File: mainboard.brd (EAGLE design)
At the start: 90.2 x 95.9 mm, 6 parts, among them U1 ATMEGA2560AU, U2 ITG-3200

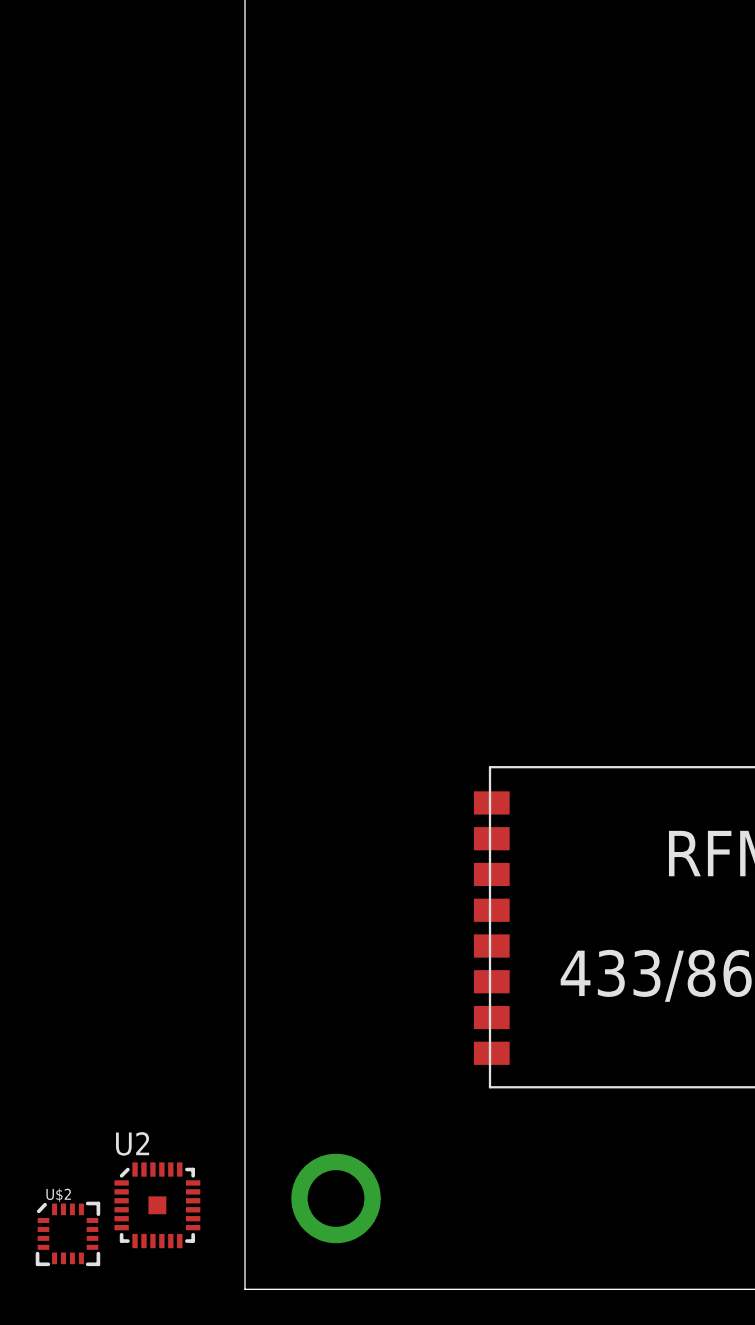
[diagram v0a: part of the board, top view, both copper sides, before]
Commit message: rename main board
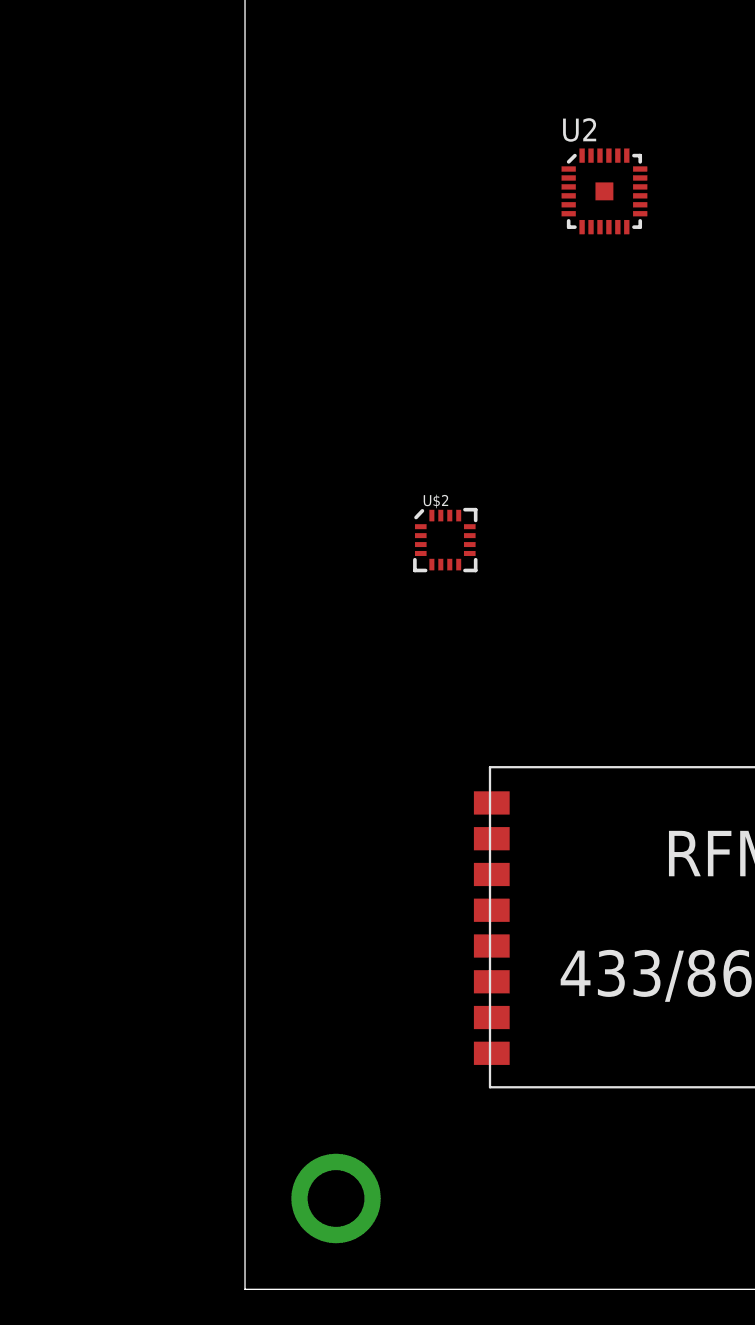
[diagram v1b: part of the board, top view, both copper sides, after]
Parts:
- moved U2 62.0 mm to (20.1, 61.4)
- moved U$2 44.2 mm to (11.2, 41.9)
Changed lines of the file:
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@@
 <element name="U1" library="SparkFun-DigitalIC" package="TQFP100" value="ATMEGA2560AU" x="45.7" y="44.1"/>
 <element name="U$1" library="RFM23BP" package="RFM23BP" value="RFM23BP" x="29.7" y="20.7"/>
-<element name="U2" library="SparkFun-Sensors" package="QFN-24" value="ITG-3200" x="-4.9" y="4.7"/>
-<element name="U$2" library="SparkFun-Sensors" package="16LPCC" value="HMC5883LSMD" x="-9.9" y="3.1"/>
+<element name="U2" library="SparkFun-Sensors" package="QFN-24" value="ITG-3200" x="20.1" y="61.4"/>
+<element name="U$2" library="SparkFun-Sensors" package="16LPCC" value="HMC5883LSMD" x="11.2" y="41.9"/>
 </elements>
 <signals>

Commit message: Added documentation
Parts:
- added IC1: FT232RLSSOP, SparkFun:SSOP28DB
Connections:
- new net GND18: IC1.18
- new net GND21: IC1.21
- new net GND7: IC1.7
- new net VCCIO: IC1.4
- net AGND: now also IC1.25
- net VCC: now also IC1.20
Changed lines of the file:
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@@
 <element name="U2" library="SparkFun-Sensors" package="QFN-24" value="ITG-3200" x="20.1" y="61.4"/>
 <element name="U$2" library="SparkFun-Sensors" package="16LPCC" value="HMC5883LSMD" x="11.2" y="41.9"/>
+<element name="IC1" library="SparkFun" package="SSOP28DB" value="FT232RLSSOP" x="66.2" y="61.6"/>
 </elements>
 <signals>
@@
 <signal name="AGND">
 <contactref element="U1" pad="99"/>
+<contactref element="IC1" pad="25"/>
+<wire x1="63.925" y1="65.256" x2="40.2" y2="52.1" width="0" layer="19" extent="1-1"/>
 </signal>
 <signal name="AVCC">
@@
 <contactref element="U1" pad="10"/>
 <contactref element="U$1" pad="VCC"/>
+<contactref element="IC1" pad="20"/>
 <wire x1="46.6" y1="21.2" x2="37.7" y2="45.6" width="0" layer="19" extent="1-1"/>
+<wire x1="67.175" y1="65.256" x2="46.6" y2="21.2" width="0" layer="19" extent="1-1"/>
 </signal>
 <signal name="VCC1">
@@
 <contactref element="U1" pad="80"/>
 </signal>
+<signal name="GND7">
+<contactref element="IC1" pad="7"/>
+</signal>
+<signal name="GND18">
+<contactref element="IC1" pad="18"/>
+</signal>
+<signal name="GND21">
+<contactref element="IC1" pad="21"/>
+</signal>
+<signal name="VCCIO">
+<contactref element="IC1" pad="4"/>
+</signal>
 </signals>

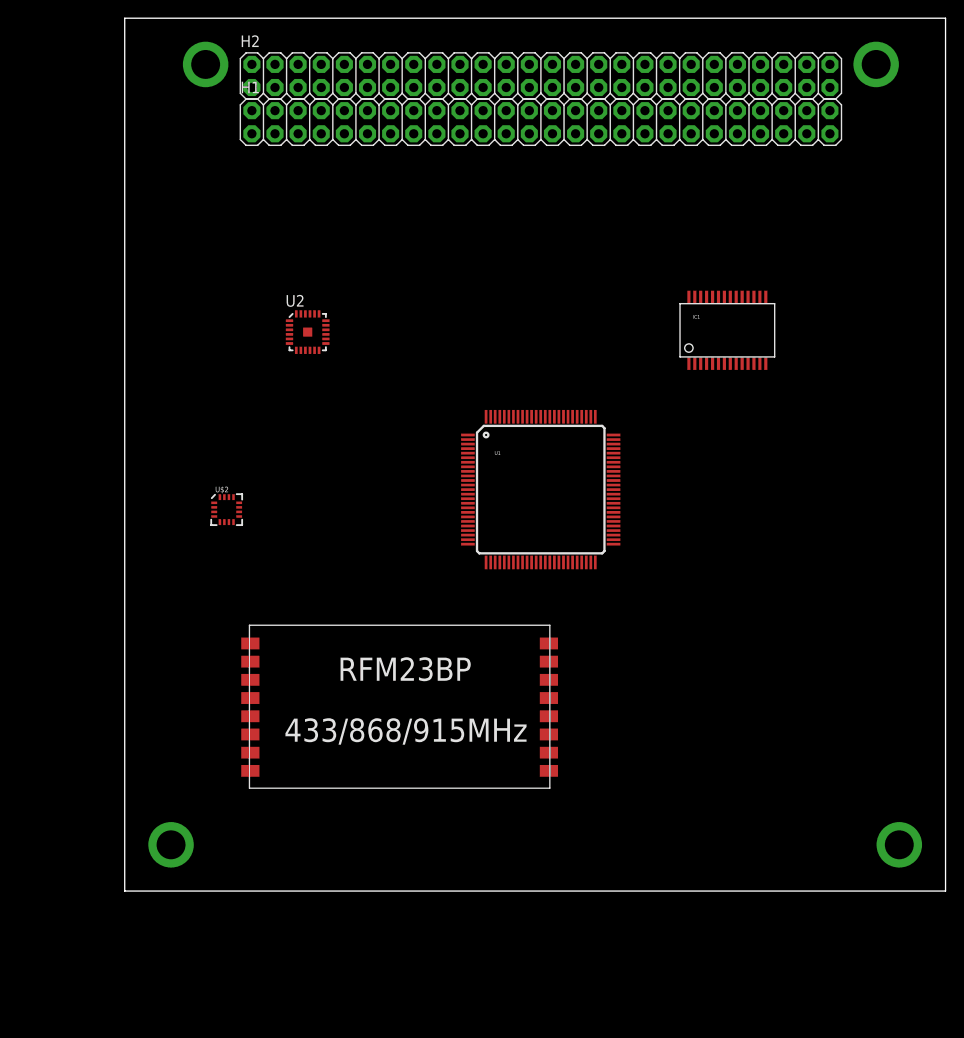
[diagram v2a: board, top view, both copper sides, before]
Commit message: Mitered corners of mainboard
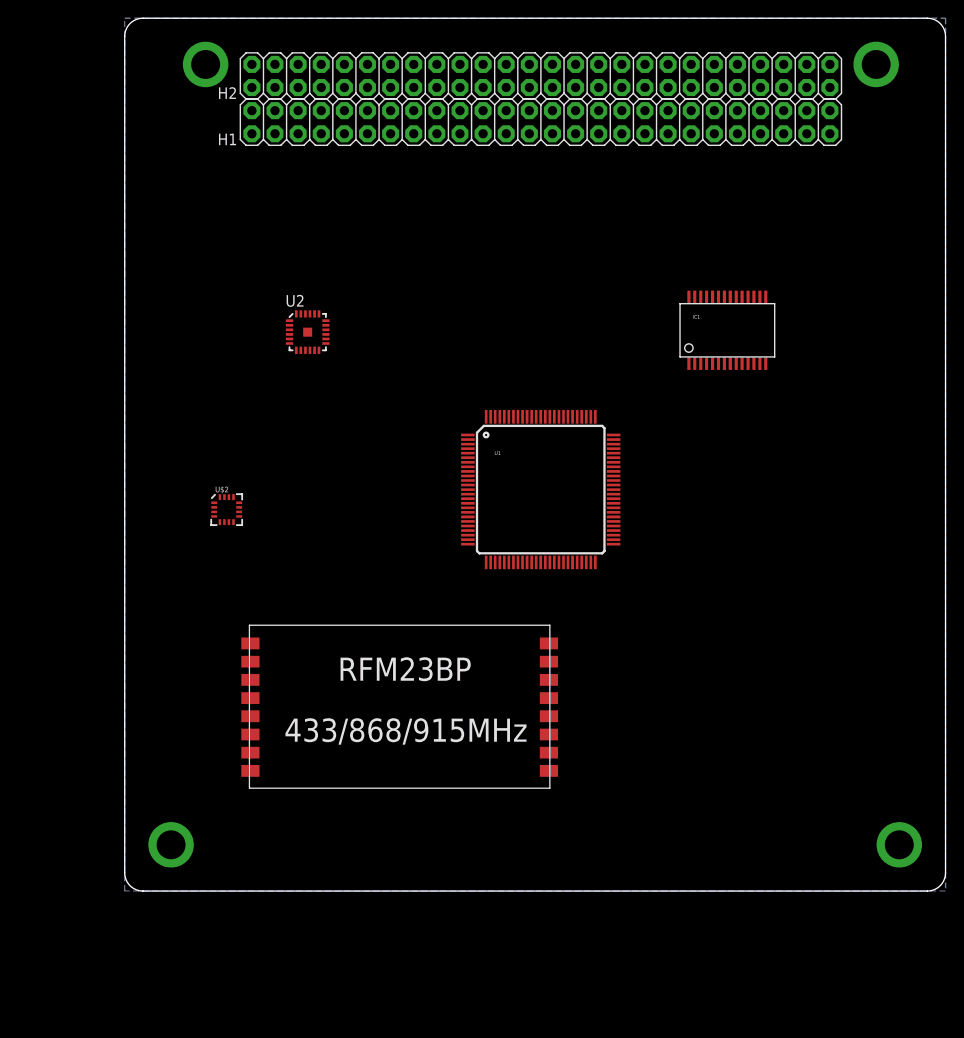
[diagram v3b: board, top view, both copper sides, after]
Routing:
- added copper zone on layer 16, net GND
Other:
- outline, holes or cut-outs redrawn
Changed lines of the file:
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@@
 <board>
 <plain>
-<wire x1="0" y1="0" x2="90.17" y2="0" width="0" layer="20"/>
-<wire x1="90.17" y1="0" x2="90.17" y2="95.885" width="0" layer="20"/>
-<wire x1="90.17" y1="95.885" x2="0" y2="95.885" width="0" layer="20"/>
-<wire x1="0" y1="95.885" x2="0" y2="0" width="0" layer="20"/>
+<wire x1="0" y1="93.885" x2="0" y2="2" width="0" layer="20"/>
+<wire x1="0" y1="2" x2="2" y2="0" width="0" layer="20" curve="90"/>
+<wire x1="2" y1="0" x2="88.17" y2="0" width="0" layer="20"/>
+<wire x1="88.17" y1="0" x2="90.17" y2="2" width="0" layer="20" curve="90"/>
+<wire x1="90.17" y1="2" x2="90.17" y2="93.885" width="0" layer="20"/>
+<wire x1="90.17" y1="93.885" x2="88.17" y2="95.885" width="0" layer="20" curve="90"/>
+<wire x1="88.17" y1="95.885" x2="2" y2="95.885" width="0" layer="20"/>
+<wire x1="2" y1="95.885" x2="0" y2="93.885" width="0" layer="20" curve="90"/>
 </plain>
 <attributes>
@@
 </class>
 </classes>
-<designrules name="default">
-<description language="de">&lt;b&gt;EAGLE Design Rules&lt;/b&gt;
+<designrules name="SSC-EAGLE-2Lyr_v1.0.0.3">
+<description language="en">&lt;b&gt;EAGLE Design Rules for *2* Layer Designs (DS)&lt;/b&gt;
 &lt;p&gt;
-Die Standard-Design-Rules sind so gewählt, dass sie für
-die meisten Anwendungen passen. Sollte ihre Platine
-besondere Anforderungen haben, treffen Sie die erforderlichen
-Einstellungen hier und speichern die Design Rules unter
-einem neuen Namen ab.</description>
-<description language="en">&lt;b&gt;EAGLE Design Rules&lt;/b&gt;
+This Sunstone Circuits 2 Layer .DRU has been set to cover our minimum requirements for our double sided products. For questions, comments, suggestions, please contact Sunstone Customer Support: &lt;p&gt;&lt;b&gt;Email:&lt;/b&gt;  mailto:support@sunstone.com&lt;br&gt;&lt;b&gt;Phone:&lt;/b&gt; 800-228-8198.&lt;p&gt; v1.1Mod10/16/07~Layers-core reversal.Distance C/D.Restring%.Supply G%.&lt;p&gt; v1.2 Mod12/06/07~Distance C/D to 20mils.&lt;p&gt;v1.3Mod12/12/07~Supply/Annulus Value to 12.5mils&lt;p&gt;1/15/08 SSC-EAGLE-2Lyr_v1.0.0.3~For Release&lt;p&gt;10/3/08 Description Edit.&lt;p&gt;
 &lt;p&gt;
-The default Design Rules have been set to cover
-a wide range of applications. Your particular design
-may have different requirements, so please make the
-necessary adjustments and save your customized
-design rules under a new name.</description>
+&lt;i&gt;Attention: Upon running the design check and making modifications, please remember to save any changes before closing the application and sending in your board file to Sunstone Circuits for conversion.&lt;i&gt;</description>
 <param name="layerSetup" value="(1*16)"/>
-<param name="mtCopper" value="0.035mm 0.035mm 0.035mm 0.035mm 0.035mm 0.035mm 0.035mm 0.035mm 0.035mm 0.035mm 0.035mm 0.035mm 0.035mm 0.035mm 0.035mm 0.035mm"/>
-<param name="mtIsolate" value="1.5mm 0.15mm 0.2mm 0.15mm 0.2mm 0.15mm 0.2mm 0.15mm 0.2mm 0.15mm 0.2mm 0.15mm 0.2mm 0.15mm 0.2mm"/>
-<param name="mdWireWire" value="8mil"/>
-<param name="mdWirePad" value="8mil"/>
-<param name="mdWireVia" value="8mil"/>
-<param name="mdPadPad" value="8mil"/>
-<param name="mdPadVia" value="8mil"/>
-<param name="mdViaVia" value="8mil"/>
-<param name="mdSmdPad" value="8mil"/>
-<param name="mdSmdVia" value="8mil"/>
-<param name="mdSmdSmd" value="8mil"/>
+<param name="mtCopper" value="0.0178mm 0.0356mm 0.0356mm 0.0356mm 0.0356mm 0.0356mm 0.0356mm 0.0356mm 0.0356mm 0.0356mm 0.0356mm 0.0356mm 0.0356mm 0.0356mm 0.0356mm 0.0178mm"/>
+<param name="mtIsolate" value="59mil 0.1499mm 0.2007mm 0.1499mm 0.2007mm 0.1499mm 0.2007mm 0.1499mm 0.2007mm 0.1499mm 0.2007mm 0.1499mm 0.2007mm 0.1499mm 0.2007mm"/>
+<param name="mdWireWire" value="6mil"/>
+<param name="mdWirePad" value="6mil"/>
+<param name="mdWireVia" value="6mil"/>
+<param name="mdPadPad" value="6mil"/>
+<param name="mdPadVia" value="6mil"/>
+<param name="mdViaVia" value="6mil"/>
+<param name="mdSmdPad" value="6mil"/>
+<param name="mdSmdVia" value="6mil"/>
+<param name="mdSmdSmd" value="6mil"/>
 <param name="mdViaViaSameLayer" value="8mil"/>
 <param name="mnLayersViaInSmd" value="2"/>
-<param name="mdCopperDimension" value="40mil"/>
-<param name="mdDrill" value="8mil"/>
+<param name="mdCopperDimension" value="20mil"/>
+<param name="mdDrill" value="16mil"/>
 <param name="mdSmdStop" value="0mil"/>
-<param name="msWidth" value="10mil"/>
-<param name="msDrill" value="24mil"/>
-<param name="msMicroVia" value="9.99mm"/>
+<param name="msWidth" value="6mil"/>
+<param name="msDrill" value="14mil"/>
+<param name="msMicroVia" value="9.9898mm"/>
 <param name="msBlindViaRatio" value="0.5"/>
 <param name="rvPadTop" value="0.25"/>
@@
 <param name="rvMicroViaOuter" value="0.25"/>
 <param name="rvMicroViaInner" value="0.25"/>
-<param name="rlMinPadTop" value="10mil"/>
-<param name="rlMaxPadTop" value="20mil"/>
-<param name="rlMinPadInner" value="10mil"/>
-<param name="rlMaxPadInner" value="20mil"/>
-<param name="rlMinPadBottom" value="10mil"/>
-<param name="rlMaxPadBottom" value="20mil"/>
+<param name="rlMinPadTop" value="8mil"/>
+<param name="rlMaxPadTop" value="999mil"/>
+<param name="rlMinPadInner" value="0mil"/>
+<param name="rlMaxPadInner" value="0mil"/>
+<param name="rlMinPadBottom" value="8mil"/>
+<param name="rlMaxPadBottom" value="999mil"/>
 <param name="rlMinViaOuter" value="8mil"/>
-<param name="rlMaxViaOuter" value="20mil"/>
-<param name="rlMinViaInner" value="8mil"/>
-<param name="rlMaxViaInner" value="20mil"/>
-<param name="rlMinMicroViaOuter" value="4mil"/>
-<param name="rlMaxMicroViaOuter" value="20mil"/>
-<param name="rlMinMicroViaInner" value="4mil"/>
-<param name="rlMaxMicroViaInner" value="20mil"/>
+<param name="rlMaxViaOuter" value="999mil"/>
+<param name="rlMinViaInner" value="0mil"/>
+<param name="rlMaxViaInner" value="0mil"/>
+<param name="rlMinMicroViaOuter" value="8mil"/>
+<param name="rlMaxMicroViaOuter" value="999mil"/>
+<param name="rlMinMicroViaInner" value="0mil"/>
+<param name="rlMaxMicroViaInner" value="0mil"/>
 <param name="psTop" value="-1"/>
 <param name="psBottom" value="-1"/>
@@
 <param name="mvStopFrame" value="1"/>
 <param name="mvCreamFrame" value="0"/>
-<param name="mlMinStopFrame" value="4mil"/>
-<param name="mlMaxStopFrame" value="4mil"/>
+<param name="mlMinStopFrame" value="3mil"/>
+<param name="mlMaxStopFrame" value="3mil"/>
 <param name="mlMinCreamFrame" value="0mil"/>
 <param name="mlMaxCreamFrame" value="0mil"/>
@@
 <param name="checkRestrict" value="1"/>
 <param name="useDiameter" value="13"/>
-<param name="maxErrors" value="50"/>
+<param name="maxErrors" value="500"/>
 </designrules>
 <autorouter>
@@
 </autorouter>
 <elements>
-<element name="H1" library="SparkFun-Connectors" package="2X26" value="PINHD-2X26" x="25.4" y="84.46"/>
-<element name="H2" library="SparkFun-Connectors" package="2X26" value="PINHD-2X26" x="25.4" y="89.54"/>
+<element name="H1" library="SparkFun-Connectors" package="2X26" value="PINHD-2X26" x="25.4" y="84.46" smashed="yes">
+<attribute name="NAME" x="10.2" y="81.935" size="1.27" layer="25" ratio="10"/>
+</element>
+<element name="H2" library="SparkFun-Connectors" package="2X26" value="PINHD-2X26" x="25.4" y="89.54" smashed="yes">
+<attribute name="NAME" x="10.2" y="87.015" size="1.27" layer="25" ratio="10"/>
+</element>
 <element name="U1" library="SparkFun-DigitalIC" package="TQFP100" value="ATMEGA2560AU" x="45.7" y="44.1"/>
 <element name="U$1" library="RFM23BP" package="RFM23BP" value="RFM23BP" x="29.7" y="20.7"/>
@@
 <via x="5.09" y="5.08" extent="1-16" drill="3.175" diameter="5"/>
 <contactref element="U1" pad="11"/>
-<wire x1="8.89" y1="90.805" x2="82.55" y2="90.805" width="0" layer="19" extent="1-1"/>
-<wire x1="85.09" y1="5.08" x2="82.55" y2="90.805" width="0" layer="19" extent="1-1"/>
-<wire x1="5.09" y1="5.08" x2="85.09" y2="5.08" width="0" layer="19" extent="1-1"/>
-<wire x1="37.7" y1="45.1" x2="5.09" y2="5.08" width="0" layer="19" extent="1-1"/>
+<polygon width="0.4064" layer="16">
+<vertex x="0" y="95.885"/>
+<vertex x="90.17" y="95.885"/>
+<vertex x="90.17" y="0"/>
+<vertex x="0" y="0"/>
+</polygon>
+<wire x1="5.09" y1="5.08" x2="37.7" y2="45.1" width="0" layer="19" extent="1-1"/>
 </signal>
 <signal name="AGND">
 <contactref element="U1" pad="99"/>
 <contactref element="IC1" pad="25"/>
-<wire x1="63.925" y1="65.256" x2="40.2" y2="52.1" width="0" layer="19" extent="1-1"/>
+<wire x1="40.2" y1="52.1" x2="63.925" y2="65.256" width="0" layer="19" extent="1-1"/>
 </signal>
 <signal name="AVCC">
@@
 <contactref element="U$1" pad="VCC"/>
 <contactref element="IC1" pad="20"/>
+<wire x1="37.7" y1="45.6" x2="67.175" y2="65.256" width="0" layer="19" extent="1-1"/>
 <wire x1="46.6" y1="21.2" x2="37.7" y2="45.6" width="0" layer="19" extent="1-1"/>
-<wire x1="67.175" y1="65.256" x2="46.6" y2="21.2" width="0" layer="19" extent="1-1"/>
 </signal>
 <signal name="VCC1">

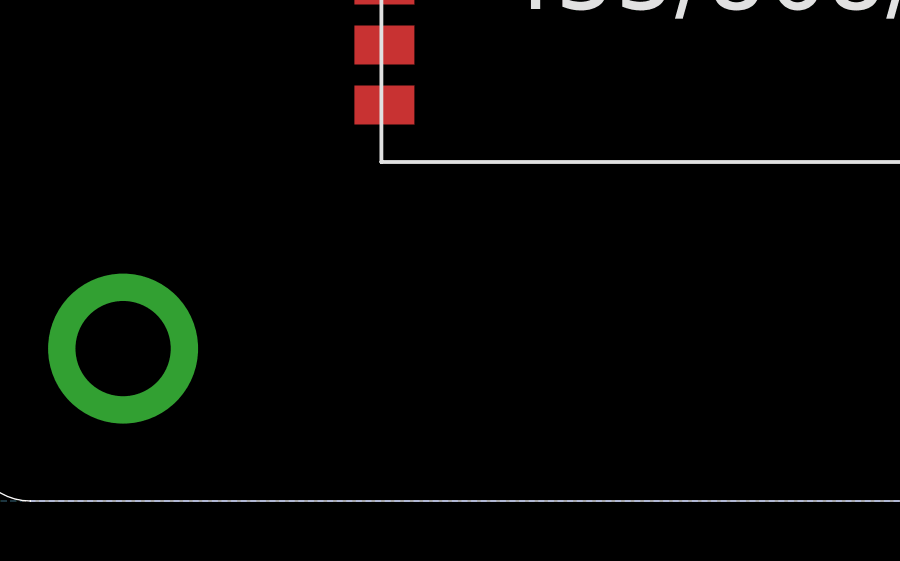
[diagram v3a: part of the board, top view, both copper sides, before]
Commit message: Added level shifter
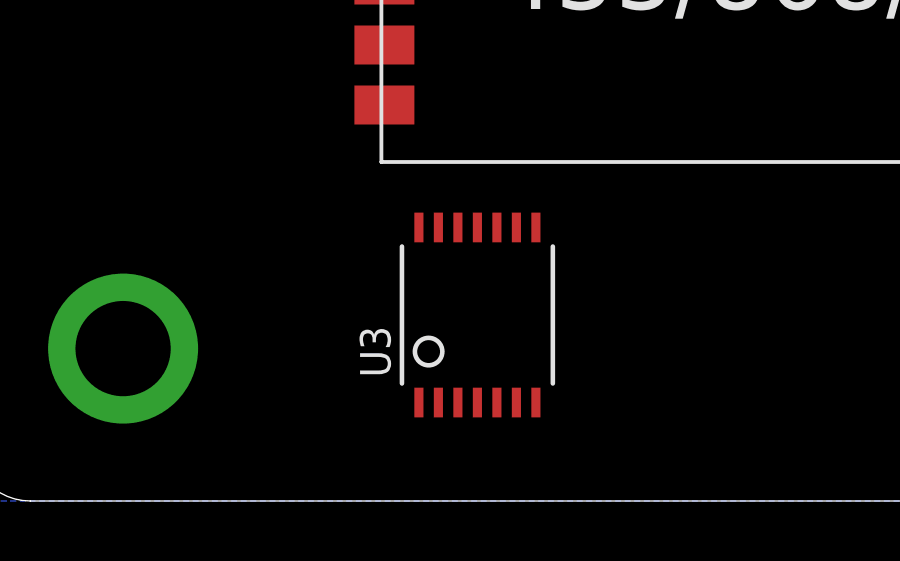
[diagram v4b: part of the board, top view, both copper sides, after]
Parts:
- added U3: (no value), SparkFun-DigitalIC:TSSOP14
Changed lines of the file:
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@@
 <element name="U$2" library="SparkFun-Sensors" package="16LPCC" value="HMC5883LSMD" x="11.2" y="41.9"/>
 <element name="IC1" library="SparkFun" package="SSOP28DB" value="FT232RLSSOP" x="66.2" y="61.6"/>
+<element name="U3" library="SparkFun-DigitalIC" package="TSSOP14" value="" x="16.9" y="6.2"/>
 </elements>
 <signals>
